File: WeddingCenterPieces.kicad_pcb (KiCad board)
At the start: 2 copper layers, 80 x 57 mm, 24 parts, among them J1 Batt_In, J2 WS2812, J3 Btn_OffBoard, SW1 Btn_OnBoard, U1 Pico, U2 TXS0101DBV, U3 MC33063AP

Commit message: Updated PCB to v1 for bulk order
Moved a trace on the bottom layer to the edge to avoid splitting the ground plane, it travels on the upper layer to get to and from the edge and then jumps to the bottom layer to cross the lines in the way.
Additionally, vertical bars have been added next to all pins that need to be connected on the surface mount pads in order to mount the RaspberryPi Pico with its castellated edges as a surface mount component.
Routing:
- net Net-(U1-GPIO28_ADC2): track 32.1 -> 69.3 mm, vias 0 -> 2
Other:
- board text added: "Shannon & Jonathan | Jan. 14th, 2024 | Wedding Center Piece v1"
- board text removed: "Shannon & Jonathan | Jan. 14th, 2024 | Wedding Center Piece v0"
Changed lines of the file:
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@@
     )
     (fp_text user "K" (at 1.08 2 90) (layer "F.SilkS")
-        (effects (font (size 1 1) (thickness 0.15)))
+        (effects (font (size 1 1) (thickness 0.15)) (justify mirror))
     )
     (fp_text user "K" (at 2.62 -0.865 90) (layer "F.Fab")
@@
   (gr_circle (center 101.674567 87.805744) (end 101.674567 88.805744)
     (stroke (width 0.15) (type default)) (fill none) (layer "B.SilkS"))
+  (gr_line (start 99.758362 74.598324) (end 99.758362 75.598324)
+    (stroke (width 0.15) (type default)) (layer "F.SilkS"))
+  (gr_line (start 99.758362 100.059221) (end 99.758362 101.059221)
+    (stroke (width 0.15) (type default)) (layer "F.SilkS"))
+  (gr_line (start 128.46613 84.65586) (end 128.46613 85.65586)
+    (stroke (width 0.15) (type default)) (layer "F.SilkS"))
+  (gr_line (start 128.46613 112.612834) (end 128.46613 113.612834)
+    (stroke (width 0.15) (type default)) (layer "F.SilkS"))
+  (gr_line (start 99.758362 94.801749) (end 99.758362 95.801749)
+    (stroke (width 0.15) (type default)) (layer "F.SilkS"))
+  (gr_line (start 128.46613 74.536801) (end 128.46613 75.536801)
+    (stroke (width 0.15) (type default)) (layer "F.SilkS"))
+  (gr_line (start 99.758362 89.808207) (end 99.758362 90.808207)
+    (stroke (width 0.15) (type default)) (layer "F.SilkS"))
+  (gr_line (start 99.758362 87.302315) (end 99.758362 88.302315)
+    (stroke (width 0.15) (type default)) (layer "F.SilkS"))
+  (gr_line (start 99.758362 92.384157) (end 99.758362 93.384157)
+    (stroke (width 0.15) (type default)) (layer "F.SilkS"))
+  (gr_line (start 128.46613 99.908124) (end 128.46613 100.908124)
+    (stroke (width 0.15) (type default)) (layer "F.SilkS"))
+  (gr_line (start 128.46613 79.586294) (end 128.46613 80.586294)
+    (stroke (width 0.15) (type default)) (layer "F.SilkS"))
+  (gr_line (start 128.46613 69.400734) (end 128.46613 70.400734)
+    (stroke (width 0.15) (type default)) (layer "F.SilkS"))
+  (gr_line (start 128.46613 71.88039) (end 128.46613 72.88039)
+    (stroke (width 0.15) (type default)) (layer "F.SilkS"))
+  (gr_line (start 99.758362 112.689274) (end 99.758362 113.689274)
+    (stroke (width 0.15) (type default)) (layer "F.SilkS"))
+  (gr_line (start 128.46613 87.262395) (end 128.46613 88.262395)
+    (stroke (width 0.15) (type default)) (layer "F.SilkS"))
   (gr_arc (start 163.5 67) (mid 165.267767 67.732233) (end 166 69.5)
     (stroke (width 0.1) (type default)) (layer "Edge.Cuts"))
@@
     (effects (font (size 1 1) (thickness 0.15)) (justify left bottom))
   )
-  (gr_text "Shannon & Jonathan | Jan. 14th, 2024 | Wedding Center Piece v0" (at 86.847969 123.083018) (layer "F.SilkS")
+  (gr_text "Shannon & Jonathan | Jan. 14th, 2024 | Wedding Center Piece v1" (at 86.847969 123.083018) (layer "F.SilkS")
     (effects (font (size 1.5 1.5) (thickness 0.3) bold) (justify left bottom))
   )
@@
   (segment (start 141.974366 106.025634) (end 139.499504 106.025634) (width 0.75) (layer "F.Cu") (net 7))
   (segment (start 147.74 94.18) (end 145.2 94.18) (width 0.75) (layer "F.Cu") (net 7))
+  (segment (start 122.78 85.22) (end 118.987701 81.427701) (width 0.25) (layer "F.Cu") (net 8))
+  (segment (start 147 70) (end 147 84.46) (width 0.25) (layer "F.Cu") (net 8))
+  (segment (start 118.987701 81.427701) (end 118.987701 69.012299) (width 0.25) (layer "F.Cu") (net 8))
   (segment (start 149.631664 90.573721) (end 149.631664 87.091664) (width 0.25) (layer "F.Cu") (net 8))
   (segment (start 149.631664 87.091664) (end 149.54 87) (width 0.25) (layer "F.Cu") (net 8))
-  (segment (start 146.54 84) (end 124 84) (width 0.25) (layer "B.Cu") (net 8))
-  (segment (start 149.54 87) (end 146.54 84) (width 0.25) (layer "B.Cu") (net 8))
-  (segment (start 124 84) (end 122.78 85.22) (width 0.25) (layer "B.Cu") (net 8))
+  (segment (start 147 84.46) (end 149.54 87) (width 0.25) (layer "F.Cu") (net 8))
+  (via (at 118.987701 69.012299) (size 0.8) (drill 0.4) (layers "F.Cu" "B.Cu") (net 8))
+  (via (at 147 70) (size 0.8) (drill 0.4) (layers "F.Cu" "B.Cu") (net 8))
+  (segment (start 118.987701 69.012299) (end 120 68) (width 0.25) (layer "B.Cu") (net 8))
+  (segment (start 146 68) (end 147 69) (width 0.25) (layer "B.Cu") (net 8))
+  (segment (start 147 69) (end 147 70) (width 0.25) (layer "B.Cu") (net 8))
+  (segment (start 120 68) (end 146 68) (width 0.25) (layer "B.Cu") (net 8))
   (segment (start 133.1375 92.95) (end 132.475 92.95) (width 0.25) (layer "F.Cu") (net 9))
   (segment (start 132 92.475) (end 132 86.357104) (width 0.25) (layer "F.Cu") (net 9))

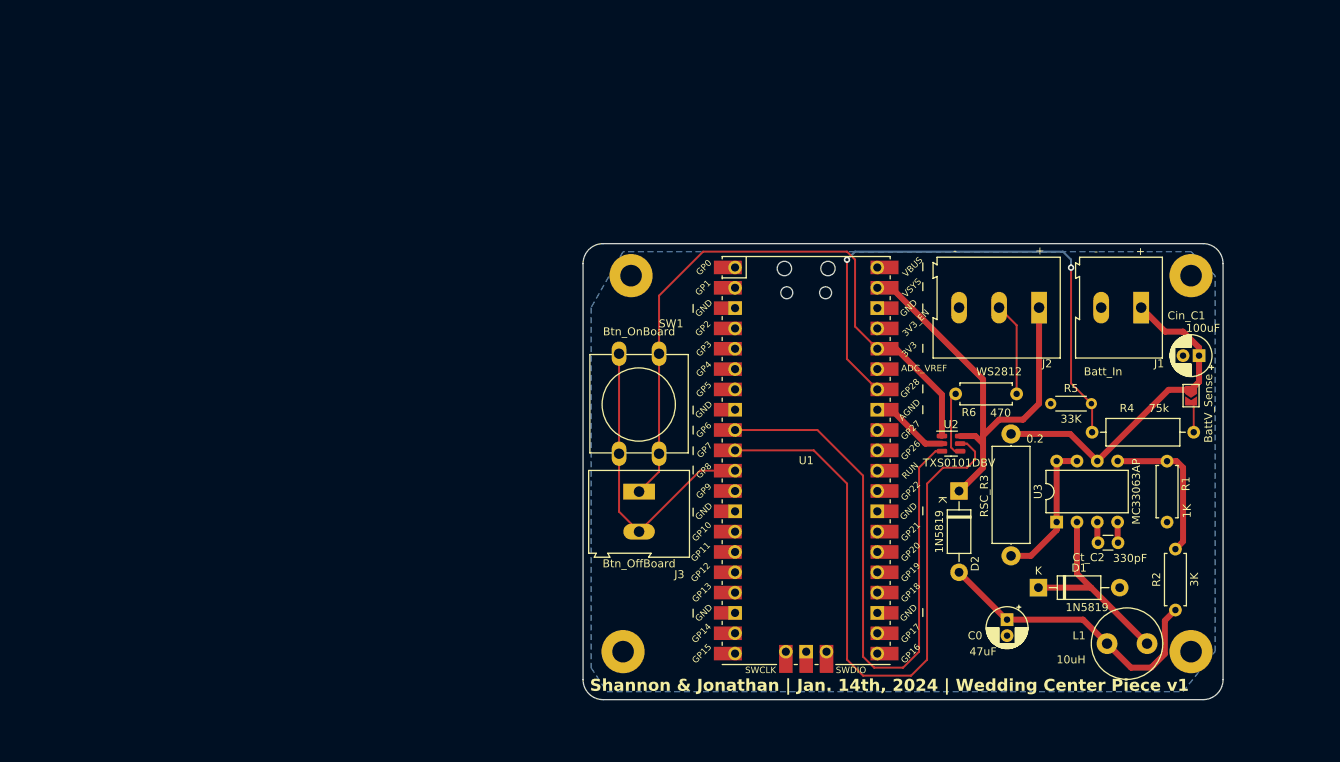
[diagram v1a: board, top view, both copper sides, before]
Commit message: WIP: Updated SK6812Mini to SK6812Mini-E and remapped ref des keys between PCB and Schematic.
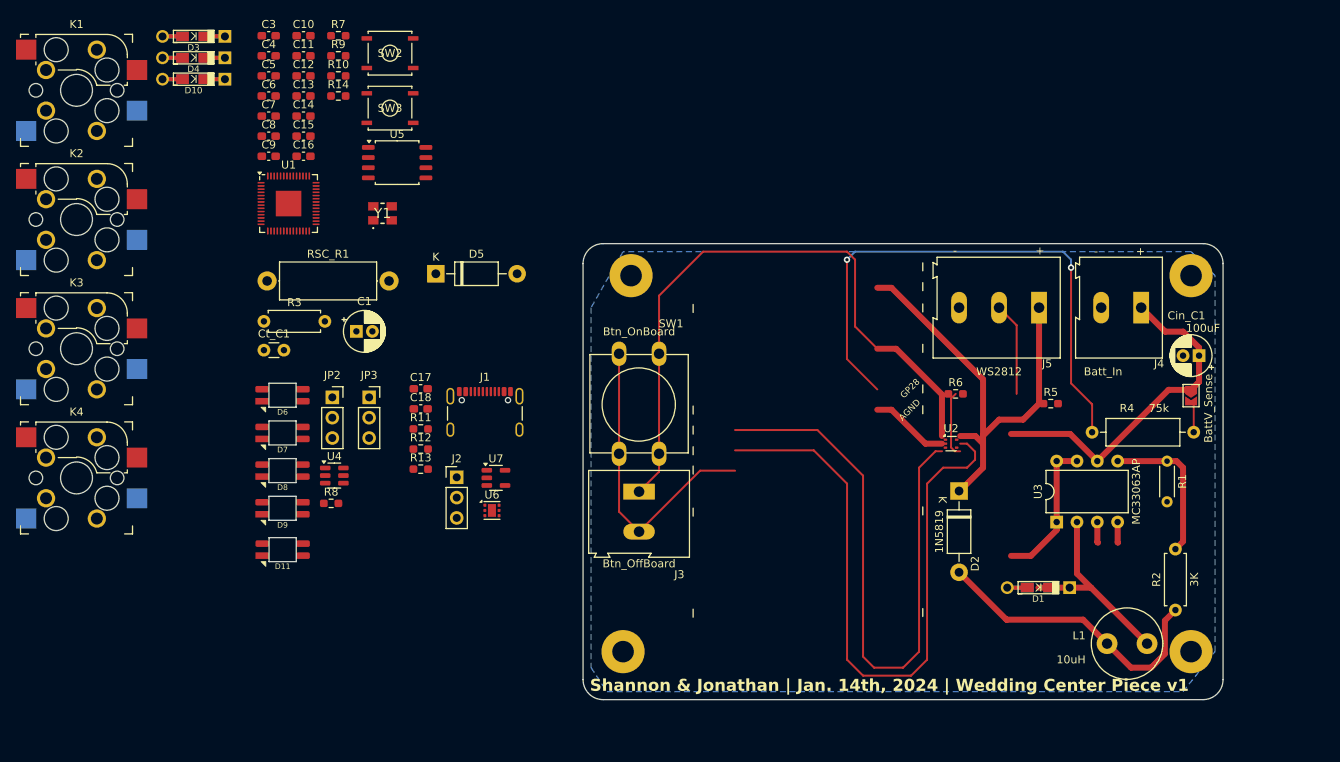
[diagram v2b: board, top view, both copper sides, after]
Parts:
- removed C0: 47uF, Capacitor_THT:CP_Radial_D5.0mm_P2.00mm
- removed Ct_C2: 330pF, Capacitor_THT:C_Disc_D3.0mm_W1.6mm_P2.50mm
- removed RSC_R3: 0.2, Resistor_THT:R_Axial_DIN0414_L11.9mm_D4.5mm_P15.24mm_Horizontal
- added C1: 47uF, Capacitor_THT:CP_Radial_D5.0mm_P2.00mm, F.Cu at (57.7, 78.0)
- added C10: 1μF, Capacitor_SMD:C_0603_1608Metric_Pad1.08x0.95mm_HandSolder, F.Cu at (51.1, 41.0)
- added C11: 1μF, Capacitor_SMD:C_0603_1608Metric_Pad1.08x0.95mm_HandSolder, F.Cu at (51.1, 43.5)
- added C12: 100nF, Capacitor_SMD:C_0603_1608Metric_Pad1.08x0.95mm_HandSolder, F.Cu at (51.1, 46.0)
- added C13: 100nF, Capacitor_SMD:C_0603_1608Metric_Pad1.08x0.95mm_HandSolder, F.Cu at (51.1, 48.5)
- added C14: 15pF, Capacitor_SMD:C_0603_1608Metric_Pad1.08x0.95mm_HandSolder, F.Cu at (51.1, 51.1)
- added C15: 15pF, Capacitor_SMD:C_0603_1608Metric_Pad1.08x0.95mm_HandSolder, F.Cu at (51.1, 53.6)
- added C16: 100nF, Capacitor_SMD:C_0603_1608Metric_Pad1.08x0.95mm_HandSolder, F.Cu at (51.1, 56.1)
- added C17: 1μF, Capacitor_SMD:C_0603_1608Metric_Pad1.08x0.95mm_HandSolder, F.Cu at (65.7, 85.1)
- added C18: 1μF, Capacitor_SMD:C_0603_1608Metric_Pad1.08x0.95mm_HandSolder, F.Cu at (65.7, 87.7)
- added C3: 100nF, Capacitor_SMD:C_0603_1608Metric_Pad1.08x0.95mm_HandSolder, F.Cu at (46.7, 41.0)
- added C4: 100nF, Capacitor_SMD:C_0603_1608Metric_Pad1.08x0.95mm_HandSolder, F.Cu at (46.7, 43.5)
- added C5: 100nF, Capacitor_SMD:C_0603_1608Metric_Pad1.08x0.95mm_HandSolder, F.Cu at (46.7, 46.0)
- added C6: 100nF, Capacitor_SMD:C_0603_1608Metric_Pad1.08x0.95mm_HandSolder, F.Cu at (46.7, 48.5)
- added C7: 100nF, Capacitor_SMD:C_0603_1608Metric_Pad1.08x0.95mm_HandSolder, F.Cu at (46.7, 51.1)
- added C8: 100nF, Capacitor_SMD:C_0603_1608Metric_Pad1.08x0.95mm_HandSolder, F.Cu at (46.7, 53.6)
- added C9: 100nF, Capacitor_SMD:C_0603_1608Metric_Pad1.08x0.95mm_HandSolder, F.Cu at (46.7, 56.1)
- added Ct_C1: 330pF, Capacitor_THT:C_Disc_D3.0mm_W1.6mm_P2.50mm, F.Cu at (46.1, 80.3)
- added D10: DIODE, keebio:Diode-dual, F.Cu at (37.3, 46.4)
- added D11: ~, Extra:SK6812-MINI-E_ReverseMount, F.Cu at (48.5, 105.2)
- added D3: DIODE, keebio:Diode-dual, F.Cu at (37.3, 41.1)
- added D4: DIODE, keebio:Diode-dual, F.Cu at (37.3, 43.8)
- added D5: 1N5819, Diode_THT:D_DO-41_SOD81_P10.16mm_Horizontal, F.Cu at (67.6, 70.8)
- added D6: ~, Extra:SK6812-MINI-E_ReverseMount, F.Cu at (48.4, 86.0)
- added D7: ~, Extra:SK6812-MINI-E_ReverseMount, F.Cu at (48.4, 90.7)
- added D8: ~, Extra:SK6812-MINI-E_ReverseMount, F.Cu at (48.4, 95.4)
- added D9: ~, Extra:SK6812-MINI-E_ReverseMount, F.Cu at (48.4, 100.1)
- added J1: USB_C_Receptacle_USB2.0_16P, Connector_USB:USB_C_Receptacle_GCT_USB4105-xx-A_16P_TopMnt_Horizontal, F.Cu at (73.7, 89.2)
- added J2: DBG, Connector_PinHeader_2.54mm:PinHeader_1x03_P2.54mm_Vertical, F.Cu at (70.2, 96.2)
- added JP2: LED_POWER, Connector_PinSocket_2.54mm:PinSocket_1x03_P2.54mm_Vertical, F.Cu at (54.7, 86.2)
- added JP3: LED_DRIVE, Connector_PinSocket_2.54mm:PinSocket_1x03_P2.54mm_Vertical, F.Cu at (59.3, 86.2)
- added K1: SW_Push, keyswitches:Kailh_socket_MX_optional_reversible, F.Cu at (22.7, 47.8)
- added K2: SW_Push, keyswitches:Kailh_socket_MX_optional_reversible, F.Cu at (22.7, 64.0)
- added K3: SW_Push, keyswitches:Kailh_socket_MX_optional_reversible, F.Cu at (22.7, 80.1)
- added K4: SW_Push, keyswitches:Kailh_socket_MX_optional_reversible, F.Cu at (22.7, 96.3)
- added R10: 1k, Resistor_SMD:R_0603_1608Metric_Pad0.98x0.95mm_HandSolder, F.Cu at (55.4, 46.0)
- added R11: 5.1k, Resistor_SMD:R_0603_1608Metric_Pad0.98x0.95mm_HandSolder, F.Cu at (65.7, 90.2)
- added R12: 5.1k, Resistor_SMD:R_0603_1608Metric_Pad0.98x0.95mm_HandSolder, F.Cu at (65.7, 92.7)
- added R13: 10k, Resistor_SMD:R_0603_1608Metric_Pad0.98x0.95mm_HandSolder, F.Cu at (65.7, 95.2)
- added R14: 10k, Resistor_SMD:R_0603_1608Metric_Pad0.98x0.95mm_HandSolder, F.Cu at (55.4, 48.5)
- added R3: 1K, Resistor_THT:R_Axial_DIN0207_L6.3mm_D2.5mm_P7.62mm_Horizontal, F.Cu at (46.1, 76.7)
- added R7: 1k, Resistor_SMD:R_0603_1608Metric_Pad0.98x0.95mm_HandSolder, F.Cu at (55.4, 41.0)
- added R8: 470, Resistor_SMD:R_0603_1608Metric_Pad0.98x0.95mm_HandSolder, F.Cu at (54.5, 99.5)
- added R9: 10k, Resistor_SMD:R_0603_1608Metric_Pad0.98x0.95mm_HandSolder, F.Cu at (55.4, 43.5)
- added RSC_R1: 0.2, Resistor_THT:R_Axial_DIN0414_L11.9mm_D4.5mm_P15.24mm_Horizontal, F.Cu at (46.5, 71.7)
- added SW2: RST, Extra:TL3342_EWI, F.Cu at (61.9, 43.2)
- added SW3: BOOT, Extra:TL3342_EWI, F.Cu at (61.9, 50.1)
- added U4: TXS0101DBV, Package_TO_SOT_SMD:SOT-23-6, F.Cu at (54.9, 96.0)
- added U5: W25Q128JVSIQ, Package_SO:SOIC-8_5.23x5.23mm_P1.27mm, F.Cu at (62.8, 56.9)
- added U6: TVS0500DRV, Package_SON:WSON-6-1EP_2x2mm_P0.65mm_EP1x1.6mm, F.Cu at (74.6, 100.3)
- added U7: AP2112K-3.3, Package_TO_SOT_SMD:SOT-23-5, F.Cu at (75.1, 96.3)
- added Y1: 12MHz, Extra:ABM8272T3, F.Cu at (60.9, 63.2)
- D1: value 1N5819 -> DIODE; footprint Diode_THT:D_DO-41_SOD81_P10.16mm_Horizontal -> keebio:Diode-dual
- R1: value 1K -> 33K; footprint Resistor_THT:R_Axial_DIN0207_L6.3mm_D2.5mm_P7.62mm_Horizontal -> Resistor_THT:R_Axial_DIN0204_L3.6mm_D1.6mm_P5.08mm_Horizontal
- R5: value 33K -> 27; footprint Resistor_THT:R_Axial_DIN0204_L3.6mm_D1.6mm_P5.08mm_Horizontal -> Resistor_SMD:R_0603_1608Metric_Pad0.98x0.95mm_HandSolder
- R6: value 470 -> 27; footprint Resistor_THT:R_Axial_DIN0207_L6.3mm_D2.5mm_P7.62mm_Horizontal -> Resistor_SMD:R_0603_1608Metric_Pad0.98x0.95mm_HandSolder
- U1: value Pico -> RP2040; footprint MCU_RaspberryPi_and_Boards:RPi_Pico_SMD_TH -> Package_DFN_QFN:QFN-56-1EP_7x7mm_P0.4mm_EP3.2x3.2mm
- U2: value TXS0101DBV -> TPD2E2U06; footprint Package_TO_SOT_SMD:SOT-23-6 -> Package_TO_SOT_SMD:SOT-553
- moved U1 72.2 mm to (49.2, 62.0)
- renumbered J1 to J4, J2 to J5
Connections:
- net /Batt+ renamed /9VTo5VSupply/Batt+
- net Net-(J3-Pin_2) renamed /External Connectors/Btn-
- D1 pad 2: GND -> /Key Switches/ROW_1
- D2 pad 1: +5V -> Net-(D2-K)
- D2 pad 2: Net-(D2-A) -> GND
- J5 pad 1: +5V -> /Lighting/PowerRail
- J5 pad 2: /Data_5V -> /External Connectors/LED_Data
- L1 pad 1: Net-(D1-K) -> Net-(D2-K)
- L1 pad 2: Net-(D2-A) -> /9VTo5VSupply/+5V
- R1 pad 1: Net-(U3-Vfb) -> GND
- R1 pad 2: GND -> /9VTo5VSupply/VBatt_Sense
- R2 pad 1: Net-(D2-A) -> /9VTo5VSupply/+5V
- R4 pad 1: Net-(U1-GPIO28_ADC2) -> /9VTo5VSupply/VBatt_Sense
- R5 pad 1: GND -> Net-(U1-USB_DP)
- R5 pad 2: Net-(U1-GPIO28_ADC2) -> /Microcontroller/D+
- R6 pad 1: Net-(U2-B) -> Net-(U1-USB_DM)
- R6 pad 2: /Data_5V -> /Microcontroller/D-
- U1 pad 1: unconnected-(U1-GPIO0-Pad1) -> +3V3
- U1 pad 10: Net-(U1-GPIO7) -> +3V3
- U1 pad 13: GND -> unconnected-(U1-GPIO10-Pad13)
- U1 pad 17: unconnected-(U1-GPIO13-Pad17) -> /Key Switches/Col1
- U1 pad 18: GND -> /Key Switches/COL_2
- U1 pad 19: unconnected-(U1-GPIO14-Pad19) -> GND
- U1 pad 20: unconnected-(U1-GPIO15-Pad20) -> Net-(U1-XIN)
- U1 pad 21: unconnected-(U1-GPIO16-Pad21) -> Net-(U1-XOUT)
- U1 pad 22: unconnected-(U1-GPIO17-Pad22) -> +3V3
- U1 pad 23: GND -> /Microcontroller/+1.1V
- U1 pad 24: unconnected-(U1-GPIO18-Pad24) -> /External Connectors/SWCLK
- U1 pad 25: unconnected-(U1-GPIO19-Pad25) -> /External Connectors/SWD
- U1 pad 26: unconnected-(U1-GPIO20-Pad26) -> Net-(U1-RUN)
- U1 pad 27: unconnected-(U1-GPIO21-Pad27) -> /Key Switches/ROW_1
- U1 pad 28: GND -> /Key Switches/ROW_2
- U1 pad 3: GND -> unconnected-(U1-GPIO1-Pad3)
- U1 pad 33: GND -> +3V3
- U1 pad 34: Net-(U1-GPIO28_ADC2) -> unconnected-(U1-GPIO22-Pad34)
- U1 pad 36: +3V3 -> unconnected-(U1-GPIO24-Pad36)
- U1 pad 38: GND -> unconnected-(U1-GPIO26_ADC0-Pad38)
- U1 pad 39: +5V -> unconnected-(U1-GPIO27_ADC1-Pad39)
- U1 pad 40: unconnected-(U1-VBUS-Pad40) -> /9VTo5VSupply/VBatt_Sense
- U1 pad 42: unconnected-(U1-GND-Pad42) -> +3V3
- U1 pad 43: unconnected-(U1-SWDIO-Pad43) -> +3V3
- U1 pad 8: GND -> /Lighting/DIN_0
- U1 pad 9: Net-(U1-GPIO6) -> unconnected-(U1-GPIO7-Pad9)
- U2 pad 1: +3V3 -> GND
- U2 pad 3: Net-(U1-GPIO6) -> /External Connectors/D-
- U2 pad 4: Net-(U2-B) -> GND
- U2 pad 5: Net-(U1-GPIO7) -> /External Connectors/D+
- U3 pad 2: Net-(D1-K) -> Net-(D2-K)
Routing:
- net Net-(U1-GPIO7): track 81.9 -> 0.00 mm
- net /External Connectors/D+: track 0.00 -> 81.9 mm
- net Net-(U1-GPIO6): track 76.1 -> 0.00 mm
- net /External Connectors/D-: track 0.00 -> 76.1 mm
- net Net-(U1-GPIO28_ADC2): track 69.3 -> 0.00 mm, vias 2 -> 0
- net /9VTo5VSupply/VBatt_Sense: track 0.00 -> 69.3 mm, vias 0 -> 2
- net Net-(D2-A): track 38.1 -> 0.00 mm
- net (no net): track 0.00 -> 38.1 mm
- net /External Connectors/LED_Data: track 0.00 -> 12.0 mm
- net /Data_5V: track 12.0 -> 0.00 mm
- net Net-(U2-B): track 8.26 -> 0.00 mm
- net GND: track 12.7 -> 21.0 mm

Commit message: Placing nearly all components onto the PCB. Removing the 9Vto5V battery input stage from populating onto the PCB.
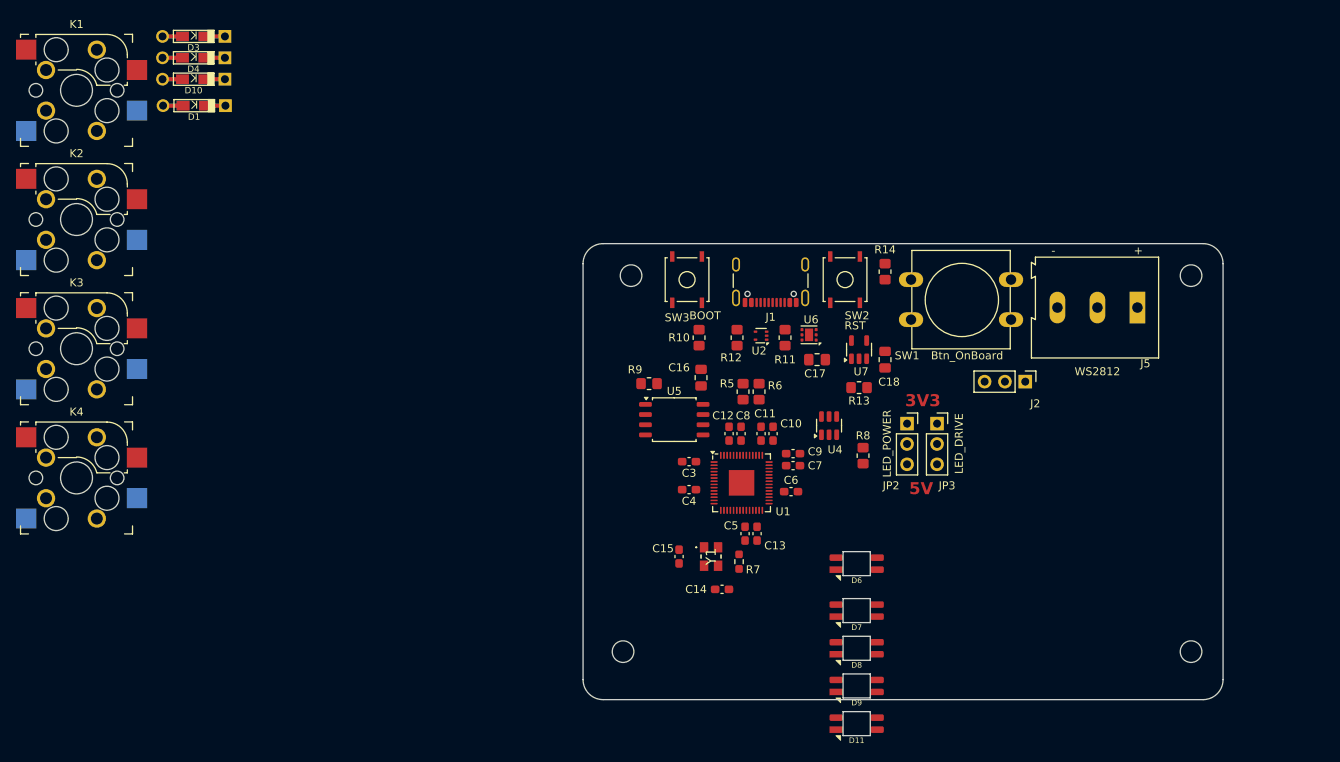
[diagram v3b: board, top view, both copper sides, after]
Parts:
- removed C1: 47uF, Capacitor_THT:CP_Radial_D5.0mm_P2.00mm
- removed Cin_C1: 100uF, Capacitor_THT:CP_Radial_D5.0mm_P2.00mm
- removed Ct_C1: 330pF, Capacitor_THT:C_Disc_D3.0mm_W1.6mm_P2.50mm
- removed D2, D5: 1N5819, Diode_THT:D_DO-41_SOD81_P10.16mm_Horizontal
- removed J3: Btn_OffBoard, TerminalBlock:TerminalBlock_Altech_AK300-2_P5.00mm
- removed J4: Batt_In, TerminalBlock:TerminalBlock_Altech_AK300-2_P5.00mm
- removed JP1: BattV_Sense, Jumper:SolderJumper-2_P1.3mm_Open_TrianglePad1.0x1.5mm
- removed L1: 10uH, Inductor_THT:L_Radial_D8.7mm_P5.00mm_Fastron_07HCP
- removed R1: 33K, Resistor_THT:R_Axial_DIN0204_L3.6mm_D1.6mm_P5.08mm_Horizontal
- removed R2: 3K, Resistor_THT:R_Axial_DIN0207_L6.3mm_D2.5mm_P7.62mm_Horizontal
- removed R3: 1K, Resistor_THT:R_Axial_DIN0207_L6.3mm_D2.5mm_P7.62mm_Horizontal
- removed R4: 75k, Resistor_THT:R_Axial_DIN0309_L9.0mm_D3.2mm_P12.70mm_Horizontal
- removed RSC_R1: 0.2, Resistor_THT:R_Axial_DIN0414_L11.9mm_D4.5mm_P15.24mm_Horizontal
- removed U3: MC33063AP, Package_DIP:DIP-8_W7.62mm
- C16, C17, C18: footprint Capacitor_SMD:C_0603_1608Metric_Pad1.08x0.95mm_HandSolder -> Capacitor_SMD:C_0805_2012Metric_Pad1.18x1.45mm_HandSolder
- D1, D10, D3, D4: footprint keebio:Diode-dual -> Keebio-Parts:Diode-dual
- H1, H2, H3, H4: value MountingHole_Pad -> MountingHole; footprint MountingHole:MountingHole_2.7mm_M2.5_Pad -> MountingHole:MountingHole_2.7mm_M2.5
- R10, R11, R12, R13, R14, R5, R6, R8, R9: footprint Resistor_SMD:R_0603_1608Metric_Pad0.98x0.95mm_HandSolder -> Resistor_SMD:R_0805_2012Metric_Pad1.20x1.40mm_HandSolder
- moved D1 121.5 mm to (37.4, 49.8)
- moved R7 82.6 mm to (105.5, 106.8), turned to 90 degrees
- moved C5 82.6 mm to (106.2, 103.2), turned to -90 degrees
- moved C6 81.9 mm to (112.0, 98.0)
- moved C14 79.0 mm to (103.4, 110.2)
- moved C13 78.8 mm to (107.8, 103.2), turned to -90 degrees
- moved C7 78.8 mm to (112.2, 94.8)
- moved C10 76.9 mm to (109.8, 90.8), turned to 90 degrees
- moved C4 75.5 mm to (99.2, 97.8), turned to 180 degrees
- moved C9 75.4 mm to (112.2, 93.2)
- moved D7 75.1 mm to (120.2, 112.9)
- moved D8 75.1 mm to (120.2, 117.6)
- moved D9 75.1 mm to (120.2, 122.3)
- moved D11 75.0 mm to (120.2, 127.0)
- moved C3 74.8 mm to (99.2, 94.2), turned to 180 degrees
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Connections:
- net /Key Switches/Col1 renamed /Key Switches/COL_1
- R5 pad 2: /Microcontroller/D+ -> /External Connectors/D+
- R6 pad 2: /Microcontroller/D- -> /External Connectors/D-
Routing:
- net +3V3: track 84.6 -> 0.00 mm
- net /External Connectors/D+: track 81.9 -> 0.00 mm
- net /External Connectors/D-: track 76.1 -> 0.00 mm
- net /9VTo5VSupply/VBatt_Sense: track 69.3 -> 0.00 mm, vias 2 -> 0
- net +5V: track 57.1 -> 0.00 mm
- net /9VTo5VSupply/Batt+: track 42.6 -> 0.00 mm
- net /External Connectors/Btn-: track 38.4 -> 0.00 mm
- net (no net): track 38.1 -> 0.00 mm
- net Net-(D1-K): track 25.4 -> 0.00 mm
- net GND: track 21.0 -> 0.00 mm
- net Net-(U3-Vfb): track 19.1 -> 0.00 mm
- net Net-(U3-DC): track 18.2 -> 0.00 mm
- net /External Connectors/LED_Data: track 12.0 -> 0.00 mm
- net Net-(JP1-B): track 3.99 -> 0.00 mm
- net Net-(U3-TC): track 2.62 -> 0.00 mm
- removed copper zone on B.Cu, net GND
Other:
- board text added: "3V3"
- board text added: "5V"
- board text removed: "AGND"
- board text removed: "GP28"
- board text removed: "Shannon & Jonathan | Jan. 14th, 2024 | Wedding Center Piece v1"
- board text removed: "אני לדודי ודודי לי"
